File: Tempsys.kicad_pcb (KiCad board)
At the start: 2 copper layers, 35 x 45 mm, 15 parts, among them J1 6P4C, J2 prog, J3 gpio, SW1 Reset, U1 E73-2G4M08S1CX, Y1 Crystal

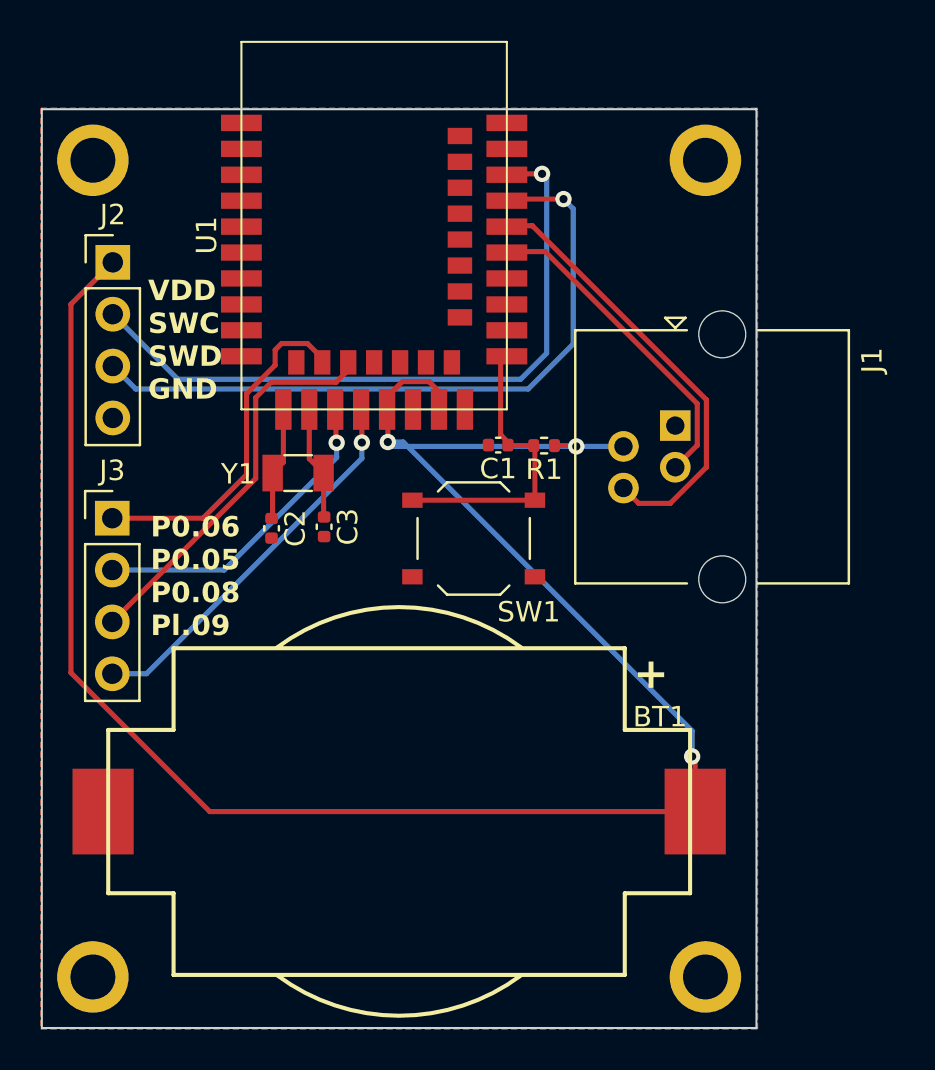
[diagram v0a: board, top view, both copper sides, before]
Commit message: Adding pull-ups and jumpers. Also fixing the RJ11 footprint
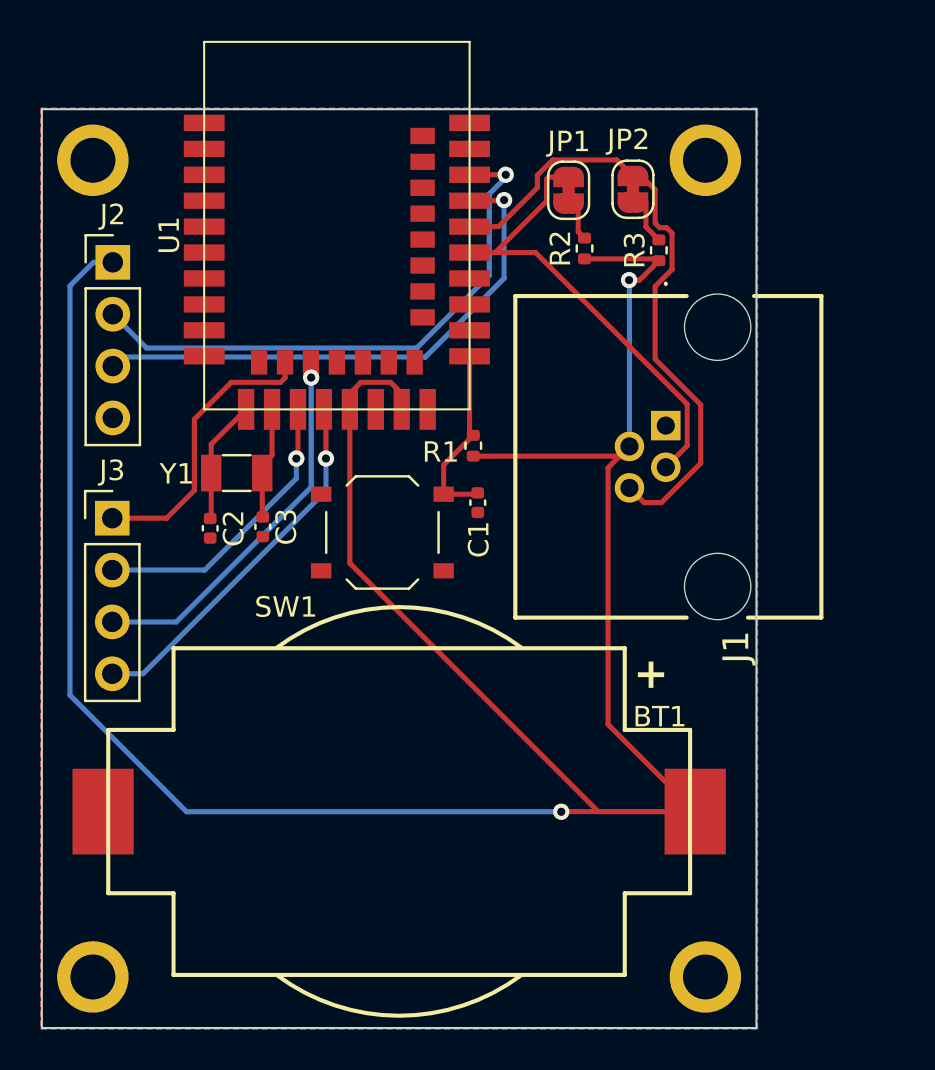
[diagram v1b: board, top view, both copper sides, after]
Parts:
- added JP1: SCL, Jumper:SolderJumper-2_P1.3mm_Bridged_RoundedPad1.0x1.5mm, F.Cu at (150.6, 73.0)
- added JP2: SDA, Jumper:SolderJumper-2_P1.3mm_Bridged_RoundedPad1.0x1.5mm, F.Cu at (153.8, 73.0)
- added R2: 10k, Resistor_SMD:R_0402_1005Metric, F.Cu at (151.4, 75.9)
- added R3: 10k, Resistor_SMD:R_0402_1005Metric, F.Cu at (155.0, 76.0)
- J1: footprint Connector_RJ:RJ14_Connfly_DS1133-S4_Horizontal -> Tempsys:438600003
- moved SW1 4.48 mm to (141.5, 89.8)
- moved R1 3.47 mm to (145.9, 85.5), turned to 90 degrees
- moved C2 3.01 mm to (133.0, 89.6)
- moved C3 3.00 mm to (135.6, 89.5)
- moved Y1 3.00 mm to (134.3, 86.9)
- moved C1 2.99 mm to (146.2, 88.3), turned to -90 degrees
- moved U1 1.82 mm to (145.8, 83.8)
- moved J1 0.46 mm to (155.4, 84.5), turned to 90 degrees
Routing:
- net VDD: track 97.6 -> 131.1 mm, vias 3 -> 2
- net /sda_pin: track 22.0 -> 30.8 mm
- net /swd_pin: track 34.3 -> 25.9 mm
- net /scl_pin: track 16.3 -> 24.3 mm
- net /swc_pin: track 34.0 -> 27.6 mm
- net /reset_pin: track 14.5 -> 9.09 mm
- net /p0.06: track 17.3 -> 14.1 mm
- net Net-(JP2-B): track 0.00 -> 2.09 mm
- net Net-(JP1-B): track 0.00 -> 1.89 mm
- net /p0.05: track 16.0 -> 14.3 mm
- net /p1.09: track 19.4 -> 18.2 mm
- net /p0.08: track 19.4 -> 18.6 mm, vias 0 -> 1
- net Net-(U1-XL2): track 5.57 -> 5.04 mm
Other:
- board text removed: "P0.06 P0.05 P0.08 Pl.09"
- board text removed: "VDD SWC SWD GND"
